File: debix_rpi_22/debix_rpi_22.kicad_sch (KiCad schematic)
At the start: 2 parts, among them J1 Conn_01x24, J3 RPi 22 Pin MIPI CSI-2

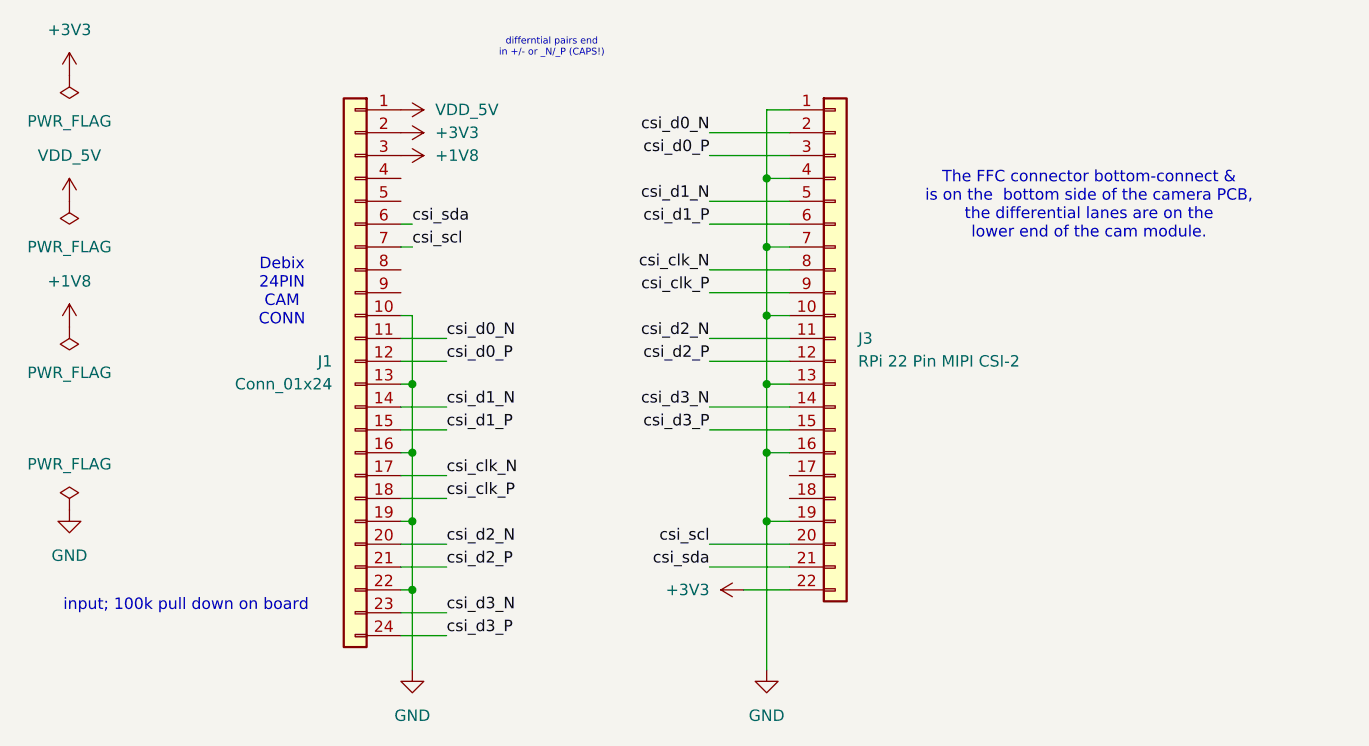
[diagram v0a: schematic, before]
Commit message: added reset/enable whatever pin other pin. Ambiguous commit message for ambiguous pin naming. =,D
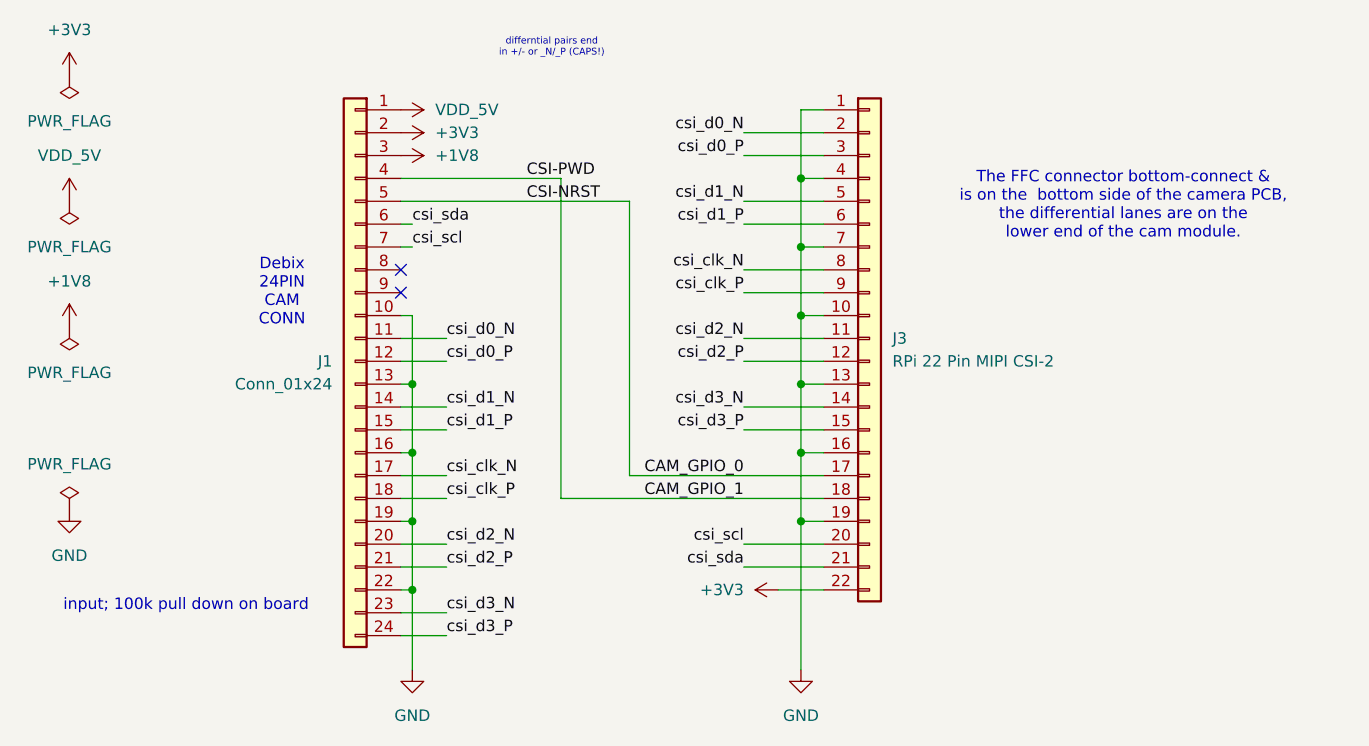
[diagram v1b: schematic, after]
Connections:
- net CAM_GPIO_1: now reaches J1.4 (Pin_4)
- net CAM_GPIO_1: now also J3.18 (Pin_18)
- net CAM_GPIO_0: now reaches J1.5 (Pin_5)
- net CAM_GPIO_0: now also J3.17 (Pin_17)
- no-connect marks 0 -> 2
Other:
- moved on the sheet: J3
